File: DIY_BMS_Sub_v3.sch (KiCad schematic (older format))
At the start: 3 parts, among them J1 Conn_02x10_Top_Bottom, J2 Conn_02x05_Top_Bottom, U1 BQ76PL536A

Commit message: Add files via upload
(re)labeled SPI-host pins to 10-pin connector. Added DIP-switch to South. Started placing decoupling capacitors.
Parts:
- added C13, C18, C19: 0.1u, Capacitor_SMD:C_0805_2012Metric_Pad1.15x1.40mm_HandSolder, symbol Device:C
- added C14, C15, C16, C17: 33p, Capacitor_SMD:C_0603_1608Metric_Pad1.05x0.95mm_HandSolder, symbol Device:C
- added H1, H2, H3, H4, H5, H6: MountingHole, MountingHole:MountingHole_3.2mm_M3, symbol Mechanical:MountingHole
- added J3, J4: Conn_02x04_Top_Bottom, Connector_Molex:Molex_Mini-Fit_Jr_5569-08A2_2x04_P4.20mm_Horizontal, symbol Connector_Generic:Conn_02x04_Top_Bottom
- added RN1: 1K_Pack08, Resistor_SMD:R_Array_Convex_8x0602, symbol Device:R_Pack08
- added SW1: SW_DIP_x01, Button_Switch_THT:SW_DIP_SPSTx01_Slide_6.7x4.1mm_W7.62mm_P2.54mm_LowProfile, symbol Switch:SW_DIP_x01
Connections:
- net labels added: ALERT_H, ALERT_N, ALERT_S, CONV_H, CONV_N, CONV_S, CS_N, CS_S, DRDY_H, DRDY_N, DRDY_S, FAULT_H, FAULT_N, FAULT_S, SCLK_H, SCLK_N, SCLK_S, SDI_N, SDI_S, SDO_N, SDO_S
- wire segments 52 -> 165
- no-connect marks 0 -> 7
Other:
- note added: "Mechanical"
- moved on the sheet: U1

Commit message: Add files via upload
Finished adding decoupling caps. Added temperature sensor (TS1).
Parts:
- added C20, C21, C23: 2.2u, Capacitor_SMD:C_0805_2012Metric_Pad1.15x1.40mm_HandSolder, symbol Device:C
- added C22: 10u, Capacitor_SMD:C_0805_2012Metric_Pad1.15x1.40mm_HandSolder, symbol Device:C
- added C24: 47p, Capacitor_SMD:C_0805_2012Metric_Pad1.15x1.40mm_HandSolder, symbol Device:C
- added R37: 1K47, Resistor_SMD:R_0603_1608Metric_Pad1.05x0.95mm_HandSolder, symbol Device:R
- added R38: 1K82, Resistor_SMD:R_0603_1608Metric_Pad1.05x0.95mm_HandSolder, symbol Device:R
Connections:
- net labels added: 5VDC, Temp+, Temp-
- wire segments 165 -> 192
- no-connect marks 7 -> 9
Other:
- note added: "NTC\n81-NXFT15XH103FA2B00\n"
- moved on the sheet: C13, C14, C15, C16, C17, C18, C19, H1, H2, H3, H4, H5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

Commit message: Add files via upload
Added 3d models for connectors (Molex). Started changing cell connections from Top-layer to IN1-layer.
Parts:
- J1: footprint Connector_Molex:Molex_Mini-Fit_Jr_5569-20A2_2x10_P4.20mm_Horizontal -> #_Connectors:Molex_Mini-Fit_Jr_5569-20A2_2x10_P4.20mm_Horizontal_with3d
- J2: footprint Connector_Molex:Molex_Mini-Fit_Jr_5569-10A2_2x05_P4.20mm_Horizontal -> #_Connectors:Molex_Mini-Fit_Jr_5569-10A2_2x05_P4.20mm_Horizontal_with3d
- J3, J4: footprint Connector_Molex:Molex_Mini-Fit_Jr_5569-08A2_2x04_P4.20mm_Horizontal -> #_Connectors:Molex_Mini-Fit_Jr_5569-08A2_2x04_P4.20mm_Horizontal_with3D
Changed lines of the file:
@@
 F 0 "J1" H 1700 2667 50  0000 C CNN
 F 1 "Conn_02x10_Top_Bottom" H 1700 2576 50  0000 C CNN
-F 2 "Connector_Molex:Molex_Mini-Fit_Jr_5569-20A2_2x10_P4.20mm_Horizontal" H 1650 2050 50  0001 C CNN
+F 2 "#_Connectors:Molex_Mini-Fit_Jr_5569-20A2_2x10_P4.20mm_Horizontal_with3d" H 1650 2050 50  0001 C CNN
 F 3 "~" H 1650 2050 50  0001 C CNN
 	1    1650 2050
@@
 F 0 "J2" H 3450 2417 50  0000 C CNN
 F 1 "Conn_02x05_Top_Bottom" H 3450 2326 50  0000 C CNN
-F 2 "Connector_Molex:Molex_Mini-Fit_Jr_5569-10A2_2x05_P4.20mm_Horizontal" H 3400 2000 50  0001 C CNN
+F 2 "#_Connectors:Molex_Mini-Fit_Jr_5569-10A2_2x05_P4.20mm_Horizontal_with3d" H 3400 2000 50  0001 C CNN
 F 3 "~" H 3400 2000 50  0001 C CNN
 	1    3400 2000
@@
 F 0 "J3" H 5150 2267 50  0000 C CNN
 F 1 "Conn_02x04_Top_Bottom" H 5150 2176 50  0000 C CNN
-F 2 "Connector_Molex:Molex_Mini-Fit_Jr_5569-08A2_2x04_P4.20mm_Horizontal" H 5100 1950 50  0001 C CNN
+F 2 "#_Connectors:Molex_Mini-Fit_Jr_5569-08A2_2x04_P4.20mm_Horizontal_with3D" H 5100 1950 50  0001 C CNN
 F 3 "~" H 5100 1950 50  0001 C CNN
 	1    5100 1950
@@
 F 0 "J4" H 7150 2267 50  0000 C CNN
 F 1 "Conn_02x04_Top_Bottom" H 7150 2176 50  0000 C CNN
-F 2 "Connector_Molex:Molex_Mini-Fit_Jr_5569-08A2_2x04_P4.20mm_Horizontal" H 7100 1950 50  0001 C CNN
+F 2 "#_Connectors:Molex_Mini-Fit_Jr_5569-08A2_2x04_P4.20mm_Horizontal_with3D" H 7100 1950 50  0001 C CNN
 F 3 "~" H 7100 1950 50  0001 C CNN
 	1    7100 1950

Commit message: Add files via upload
Finished routing board (rev.0). Organised silkscreen labels.
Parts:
- removed SW1: SW_DIP_x01, Button_Switch_THT:SW_DIP_SPSTx01_Slide_6.7x4.1mm_W7.62mm_P2.54mm_LowProfile, symbol Switch:SW_DIP_x01
- added R39: 100K, Resistor_SMD:R_0805_2012Metric_Pad1.15x1.40mm_HandSolder, symbol Device:R
- added SW1: SW_DIP_x04, Button_Switch_THT:SW_DIP_SPSTx04_Slide_9.78x12.34mm_W7.62mm_P2.54mm, symbol Switch:SW_DIP_x04
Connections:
- net labels added: SW_Bottom, SW_Host, SW_NotTop, SW_Top
- wire segments 192 -> 207
- no-connect marks 9 -> 10
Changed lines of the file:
@@
 	1    0    0    -1
 $EndComp
-Text GLabel 3800 1800 2    50   Input ~ 0
-HSEL
 Wire Notes Line
 	850  850  850  2850
@@
 Wire Wire Line
 	3800 1900 3700 1900
-Wire Wire Line
-	3800 1800 3700 1800
 Text GLabel 10350 7100 2    50   Input ~ 0
 SDI_H
@@
 	1500 5650 1600 5650
 Wire Wire Line
-	1500 5200 7000 5200
-Wire Wire Line
 	7500 5200 7500 5300
 Wire Wire Line
@@
 CONV_N
 Wire Wire Line
-	8550 4400 8550 5000
+	8550 4400 8550 4700
 Text GLabel 5500 1850 2    50   Input ~ 0
 CONV_N
@@
 Wire Wire Line
 	7000 3600 7000 3750
-Connection ~ 7000 5200
-Wire Wire Line
-	7000 5200 7500 5200
 Wire Wire Line
 	7100 4050 7000 4050
-Connection ~ 7000 4050
-Wire Wire Line
-	7000 4050 7000 5200
 Wire Wire Line
 	7450 3900 7000 3900
@@
 Wire Wire Line
 	9300 10250 9300 10400
-$Comp
-L Switch:SW_DIP_x01 SW1
-U 1 1 5FBECB4C
-P 8150 10100
-F 0 "SW1" H 8150 10367 50  0000 C CNN
-F 1 "SW_DIP_x01" H 8150 10276 50  0000 C CNN
-F 2 "Button_Switch_THT:SW_DIP_SPSTx01_Slide_6.7x4.1mm_W7.62mm_P2.54mm_LowProfile" H 8150 10100 50  0001 C CNN
-F 3 "file:///C:/Users/HenkHenk/Downloads/ds01_254-1777712%20(2).pdf" H 8150 10100 50  0001 C CNN
-F 4 "490-DS01-254-L-01BE" H 8150 10100 50  0001 C CNN "DPN"
-	1    8150 10100
-	1    0    0    -1
-$EndComp
 Wire Wire Line
 	8600 10250 8600 10400
@@
 	9300 10250 9350 10250
 Wire Wire Line
-	8600 10800 8600 10900
+	8600 10800 8600 10850
 Wire Wire Line
 	8700 10800 8700 10900
@@
 Wire Wire Line
 	9300 10800 9300 10900
-Wire Wire Line
-	8550 9750 8550 10100
-Text GLabel 7750 10100 0    50   UnSpc ~ 0
-AGND
-Wire Wire Line
-	7750 10100 7850 10100
-Wire Wire Line
-	8450 10100 8550 10100
-Connection ~ 8550 10100
-Wire Wire Line
-	8550 10100 8550 10250
+Text GLabel 4950 11050 0    50   UnSpc ~ 0
+AGND
 Wire Wire Line
 	9350 10250 9350 9750
@@
 NoConn ~ 10250 5300
 NoConn ~ 10250 5400
-Text GLabel 10650 6800 2    50   Input ~ 0
+Text GLabel 11750 6650 2    50   Input ~ 0
 HSEL
 Wire Wire Line
@@
 Wire Wire Line
 	11900 8900 12000 8900
-Wire Wire Line
-	10250 6800 10650 6800
 $Comp
 L Device:C C?
@@
 Wire Notes Line
 	850  850  8000 850
+Text GLabel 5750 10950 2    50   Input ~ 0
+SW_Host
+Text GLabel 5750 11050 2    50   Input ~ 0
+SW_Bottom
+Text GLabel 5750 10750 2    50   Input ~ 0
+SW_Top
+Wire Wire Line
+	5750 10750 5650 10750
+Wire Wire Line
+	5750 10950 5650 10950
+Wire Wire Line
+	5750 11050 5650 11050
+Wire Wire Line
+	4950 11050 5050 11050
+Text GLabel 8500 10850 0    50   Input ~ 0
+SW_Bottom
+Wire Wire Line
+	8500 10850 8600 10850
+Wire Wire Line
+	5050 10950 4950 10950
+Wire Wire Line
+	5050 10850 4950 10850
+Text GLabel 4950 10950 0    50   UnSpc ~ 0
+AGND
+Text GLabel 10950 6650 2    50   Input ~ 0
+SW_Host
+$Comp
+L Device:R R?
+U 1 1 5FCE7782
+P 11100 6800
+AR Path="/5FAF2B15/5FCE7782" Ref="R?"  Part="1"
+AR Path="/5FB201DB/5FCE7782" Ref="R?"  Part="1"
+AR Path="/5FB24C66/5FCE7782" Ref="R?"  Part="1"
+AR Path="/5FA9BBC5/5FCE7782" Ref="R?"  Part="1"
+AR Path="/5FA9D4E1/5FCE7782" Ref="R?"  Part="1"
+AR Path="/5FAA7870/5FCE7782" Ref="R?"  Part="1"
+AR Path="/5FCE7782" Ref="R39"  Part="1"
+F 0 "R39" V 11200 6700 50  0000 L CNN
+F 1 "100K" V 11300 6700 50  0000 L CNN
+F 2 "Resistor_SMD:R_0805_2012Metric_Pad1.15x1.40mm_HandSolder" V 11030 6800 50  0001 C CNN
+F 3 "~" H 11100 6800 50  0001 C CNN
+F 4 "71-CRCW0805100KFKEAC" H 11100 6800 50  0001 C CNN "DPN"
+	1    11100 6800
+	0    1    1    0
+$EndComp
+Text GLabel 11750 6500 2    50   UnSpc ~ 0
+5VDC
+Wire Wire Line
+	11750 6500 11650 6500
+Wire Wire Line
+	11650 6500 11650 6650
+Wire Wire Line
+	11250 6800 11650 6800
+Wire Wire Line
+	11750 6650 11650 6650
+Wire Wire Line
+	11650 6650 11650 6800
+Wire Wire Line
+	10850 6650 10950 6650
+NoConn ~ 3700 1800
+Connection ~ 11650 6650
+Wire Wire Line
+	10250 6800 10850 6800
+Wire Wire Line
+	10850 6650 10850 6800
+Connection ~ 10850 6800
+Wire Wire Line
+	10850 6800 10950 6800
+Text GLabel 4950 10850 0    50   Input ~ 0
+S6
+Text GLabel 8450 4700 0    50   Input ~ 0
+SW_Top
+Wire Wire Line
+	8450 4700 8550 4700
+Connection ~ 8550 4700
+Wire Wire Line
+	8550 4700 8550 5000
+$Comp
+L Switch:SW_DIP_x04 SW1
+U 1 1 5FE55576
+P 5350 10950
+F 0 "SW1" H 5350 11417 50  0000 C CNN
+F 1 "SW_DIP_x04" H 5350 11326 50  0000 C CNN
+F 2 "Button_Switch_THT:SW_DIP_SPSTx04_Slide_9.78x12.34mm_W7.62mm_P2.54mm" H 5350 10950 50  0001 C CNN
+F 3 "file:///C:/Users/HenkHenk/Downloads/ds01_254-1777712%20(5).pdf" H 5350 10950 50  0001 C CNN
+F 4 "DS01C-254-S-04BE" H 5350 10950 50  0001 C CNN "DPN"
+	1    5350 10950
+	1    0    0    -1
+$EndComp
+Text GLabel 5750 10850 2    50   Input ~ 0
+SW_NotTop
+Wire Wire Line
+	5750 10850 5650 10850
+Wire Wire Line
+	1500 5200 7500 5200
+Wire Wire Line
+	5050 10750 4950 10750
+Text GLabel 4950 10750 0    50   Input ~ 0
+S6
+Text GLabel 6900 4050 0    50   Input ~ 0
+SW_NotTop
+Wire Wire Line
+	6900 4050 7000 4050
+Connection ~ 7000 4050
+Connection ~ 8600 10850
+Wire Wire Line
+	8600 10850 8600 10900
+Wire Wire Line
+	8550 9750 8550 10250
 $EndSCHEMATC

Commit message: Add files via upload
Additional back-up before starting Rev.1
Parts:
- removed J1: Conn_02x10_Top_Bottom, #_Connectors:Molex_Mini-Fit_Jr_5569-20A2_2x10_P4.20mm_Horizontal_with3d, symbol Connector_Generic:Conn_02x10_Top_Bottom
- added F1, F2, F3, F4, F5, F6, F7: 2A, Fuse:Fuse_0603_1608Metric_Pad1.05x0.95mm_HandSolder, symbol Device:Fuse
- added J1: Conn_02x05_Top_Bottom, #_Connectors:Molex_Mini-Fit_Jr_5569-10A2_2x05_P4.20mm_Horizontal_with3d, symbol Connector_Generic:Conn_02x05_Top_Bottom
- added J5: RJ45, Connector_RJ:RJ45_Amphenol_54602-x08_Horizontal, symbol Connector:RJ45
- C13, C18, C19: DPN 710-885012207128 -> (none); LCSC (none) -> C49678
- C14, C15, C16, C17: DPN 80-C0603C330M5HACTU -> (none); LCSC (none) -> C1663
- C20, C21, C23: DPN 187-CL21B225KPFNNNE -> (none); LCSC (none) -> C49217
- C22: DPN 81-GRM21BR71A106KA3K -> (none); LCSC (none) -> C15850
- C24: DPN 80-C0805C470J5G -> (none); LCSC (none) -> C14857
- J2: DPN (none) -> 538-39-30-1100
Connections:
- net 5VDC: now also J1.1 (Pin_1)
- net AGND: now also C19.2, U1.47 (GPAI-), U1.48 (GPAI+), F1.2; no longer C19.1
- net S1: now also F2.1, J1.7 (Pin_7)
- net S2: now also F3.1, J1.8 (Pin_8)
- net S3: now also F4.2
- net S4: now also F5.1, J1.10 (Pin_10)
- net S5: now also F6.1, J1.5 (Pin_5)
- net S6: now also F7.1, J1.4 (Pin_4); no longer C13.2, U1.63 (BAT1), U1.64 (BAT2)
- net Temp-: now also J1.2 (Pin_2)
- net LDOD: now reaches J2.6 (Pin_6)
- net LDOD: now also C18.1, C20.2, U1.18 (LDOD1), U1.46 (LDOD2)
- net at C21.2, U1.17 (LDOA): now also C19.1; no longer C19.2
- new net C1: F2.2
- new net C2: F3.2
- new net C3: F4.1, J1.9 (Pin_9)
- new net C4: F5.2
- new net C5: F6.2
- new net C6: C13.2, F7.2, U1.63 (BAT1), U1.64 (BAT2)
- new net S0: F1.1, J1.6 (Pin_6)
- no-connect marks 10 -> 7
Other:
- note added: "External NTC\n81-NXFT15XH103FA2B00\n10K 1%\nB-parameter 3380K\n"
- note removed: "NTC\n81-NXFT15XH103FA2B00\n"

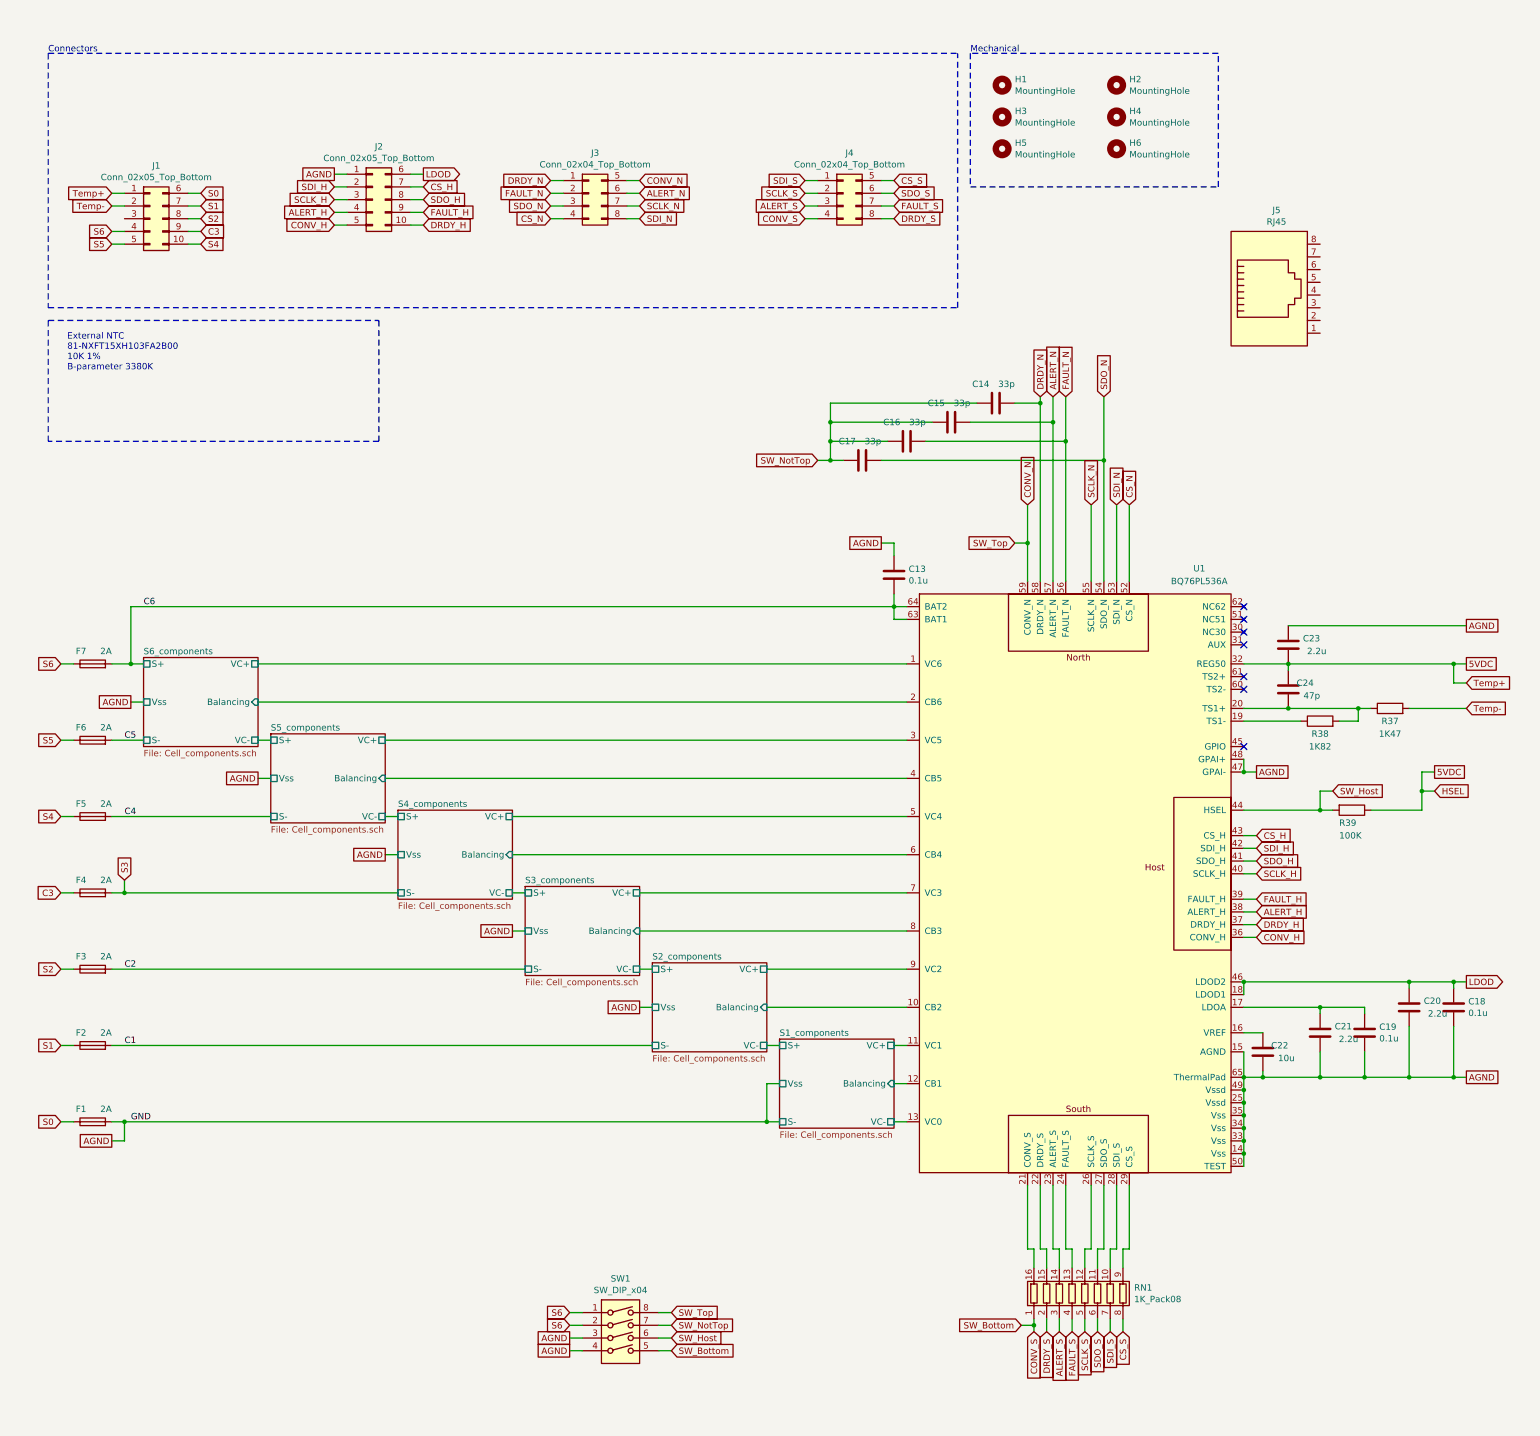
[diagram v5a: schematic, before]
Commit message: Add files via upload
Changed board dimensions. Replaced Molex connectors from MiniFit to the smaller MicroFit-type.
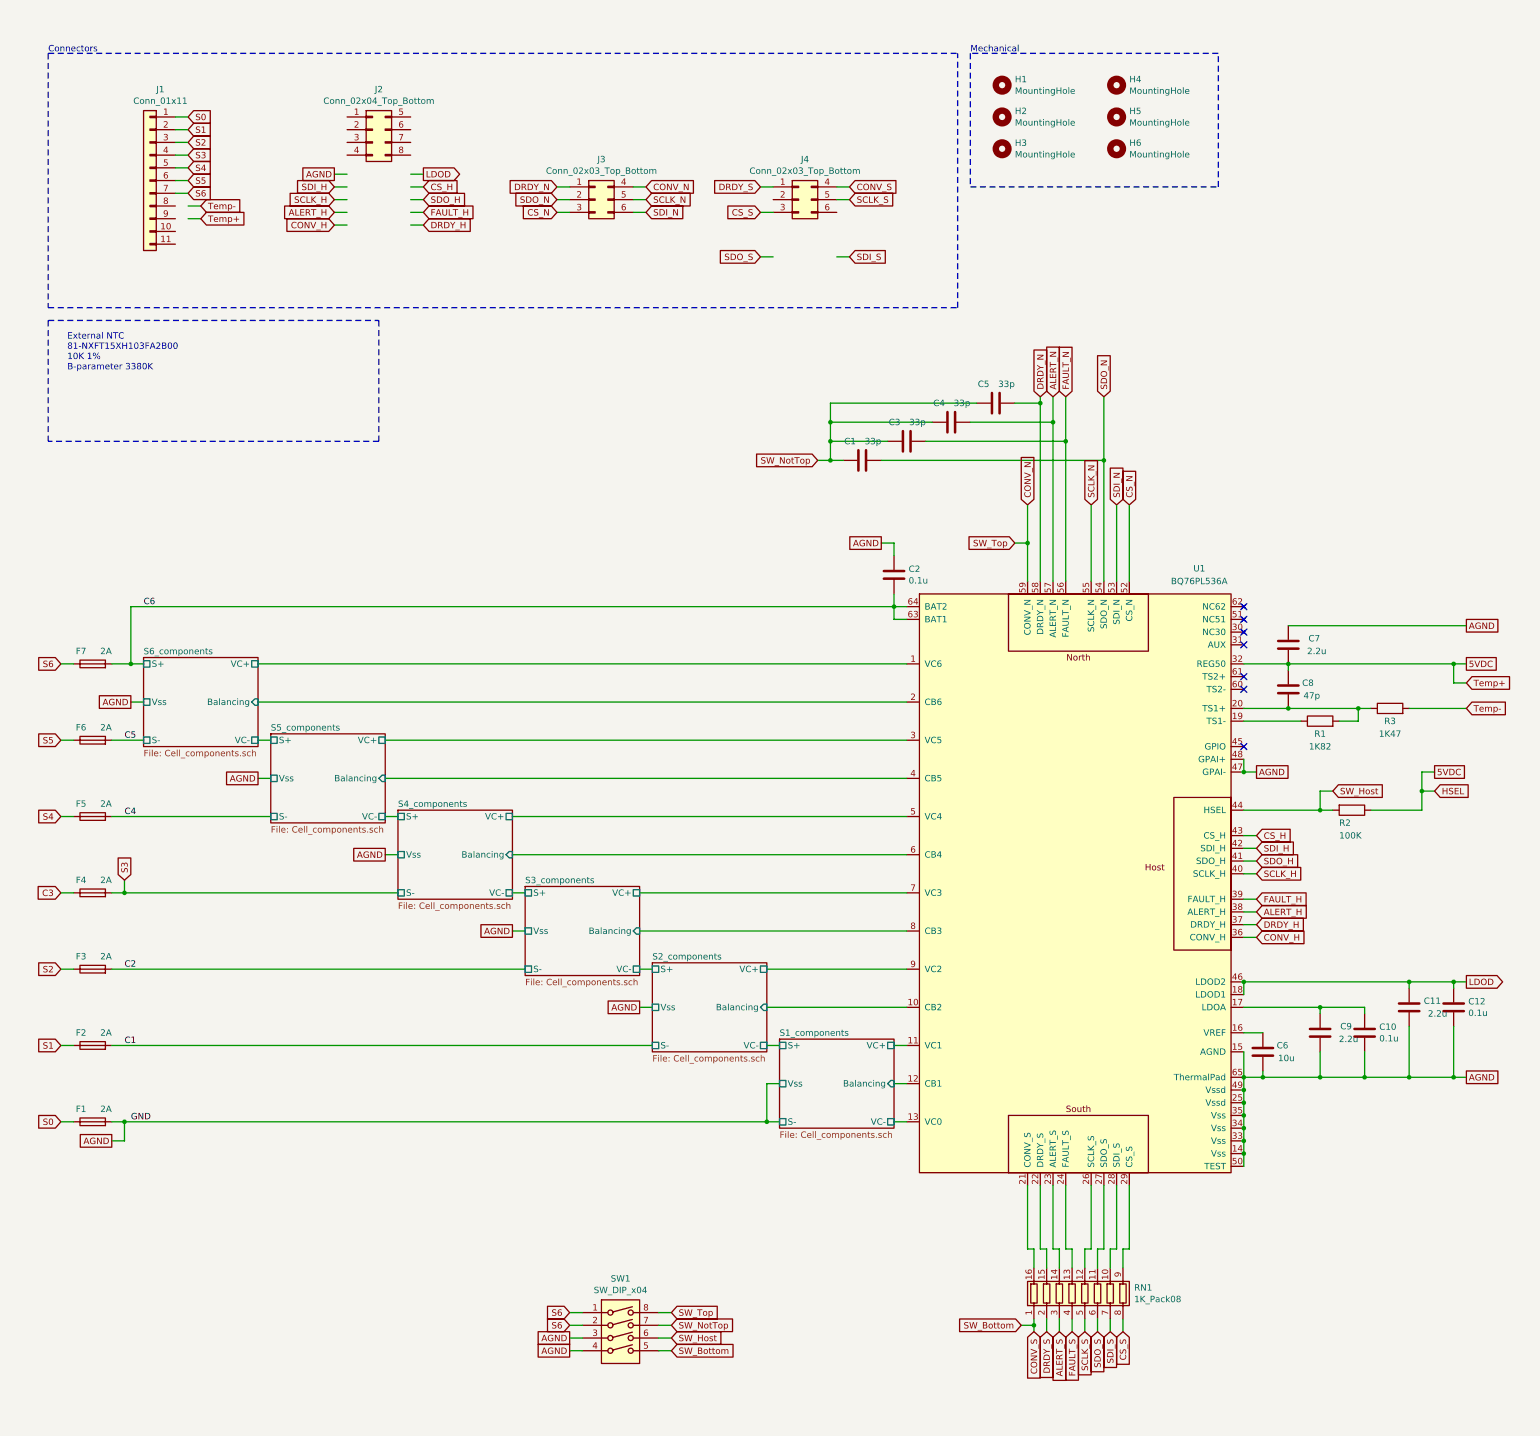
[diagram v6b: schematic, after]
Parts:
- removed J1, J2: Conn_02x05_Top_Bottom, #_Connectors:Molex_Mini-Fit_Jr_5569-10A2_2x05_P4.20mm_Horizontal_with3d, symbol Connector_Generic:Conn_02x05_Top_Bottom
- removed J3, J4: Conn_02x04_Top_Bottom, #_Connectors:Molex_Mini-Fit_Jr_5569-08A2_2x04_P4.20mm_Horizontal_with3D, symbol Connector_Generic:Conn_02x04_Top_Bottom
- removed J5: RJ45, Connector_RJ:RJ45_Amphenol_54602-x08_Horizontal, symbol Connector:RJ45
- added J1: Conn_01x11, Connector_Molex:Molex_Micro-Fit_3.0_43650-1100_1x11_P3.00mm_Horizontal, symbol Connector_Generic:Conn_01x11
- added J2: Conn_02x04_Top_Bottom, Connector_Molex:Molex_Micro-Fit_3.0_43045-0821_2x04-1MP_P3.00mm_Horizontal, symbol Connector_Generic:Conn_02x04_Top_Bottom
- added J3, J4: Conn_02x03_Top_Bottom, Connector_Molex:Molex_Micro-Fit_3.0_43045-0621_2x03-1MP_P3.00mm_Horizontal, symbol Connector_Generic:Conn_02x03_Top_Bottom
- renumbered C17 to C1, C19 to C10, C20 to C11, C18 to C12, C13 to C2, C16 to C3, C15 to C4, C14 to C5, C22 to C6, C23 to C7, C24 to C8, C21 to C9, R38 to R1, R39 to R2, R37 to R3
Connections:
- wire segments 220 -> 216
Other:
- moved on the sheet: H2, H3, H4, H5
